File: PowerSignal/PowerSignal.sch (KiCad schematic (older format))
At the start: 12 parts, among them K1 POWER, P1 DIN_4_SHIELD, P2 BNC, U1 BUF634

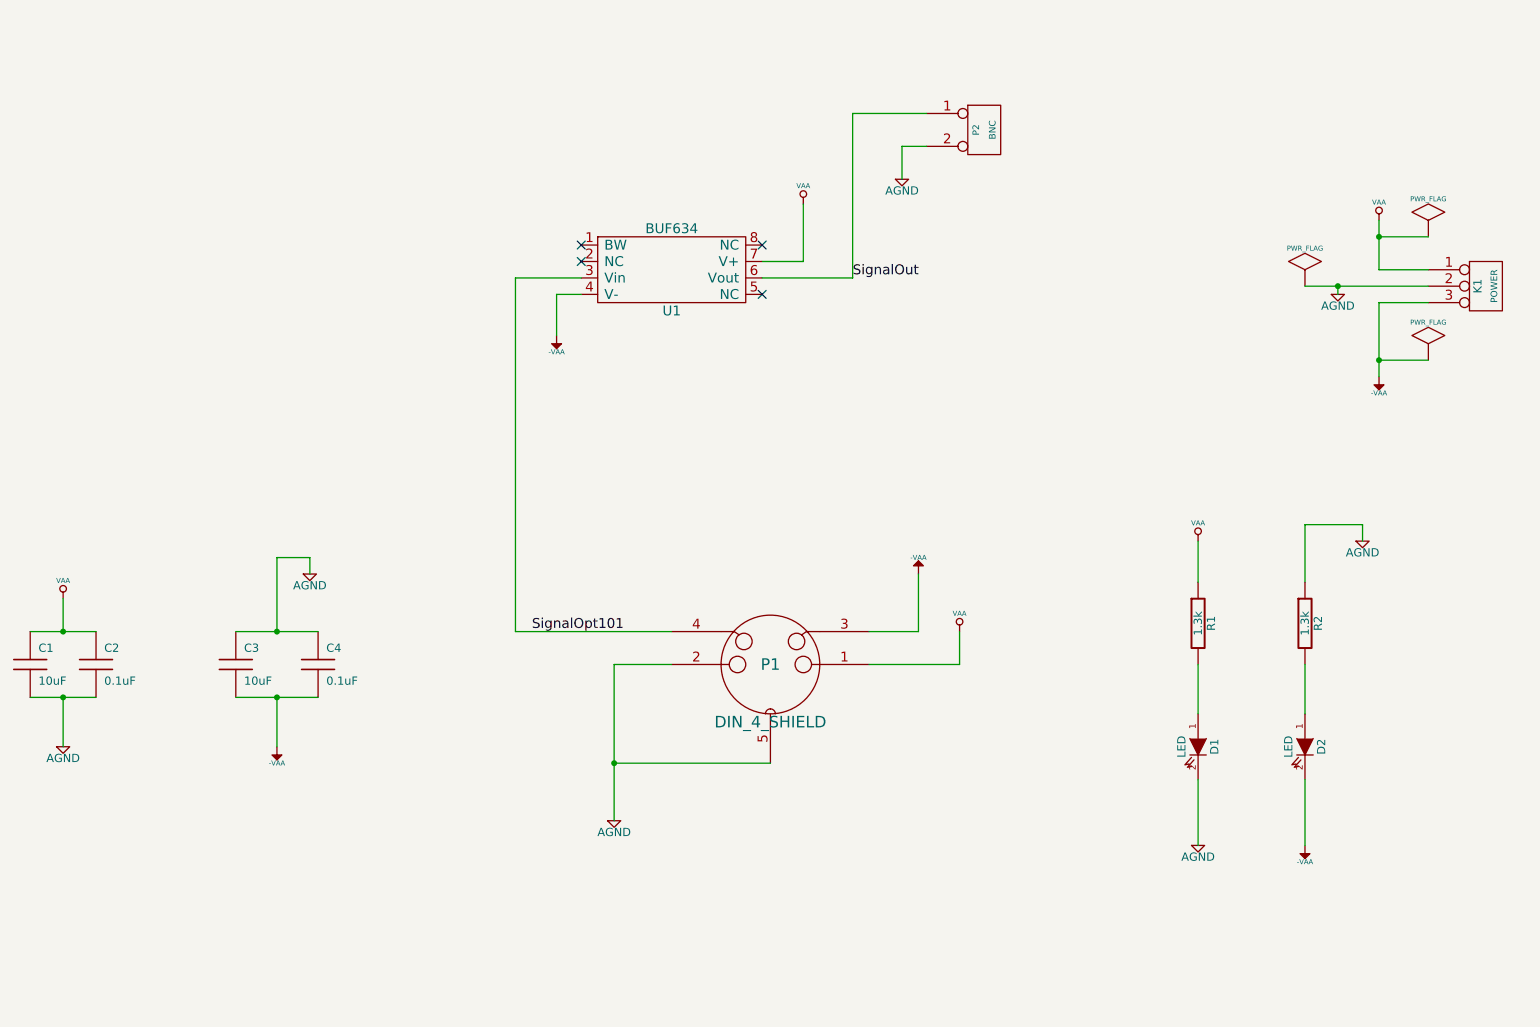
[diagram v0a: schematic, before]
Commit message: Designed PowerSupply board version 2
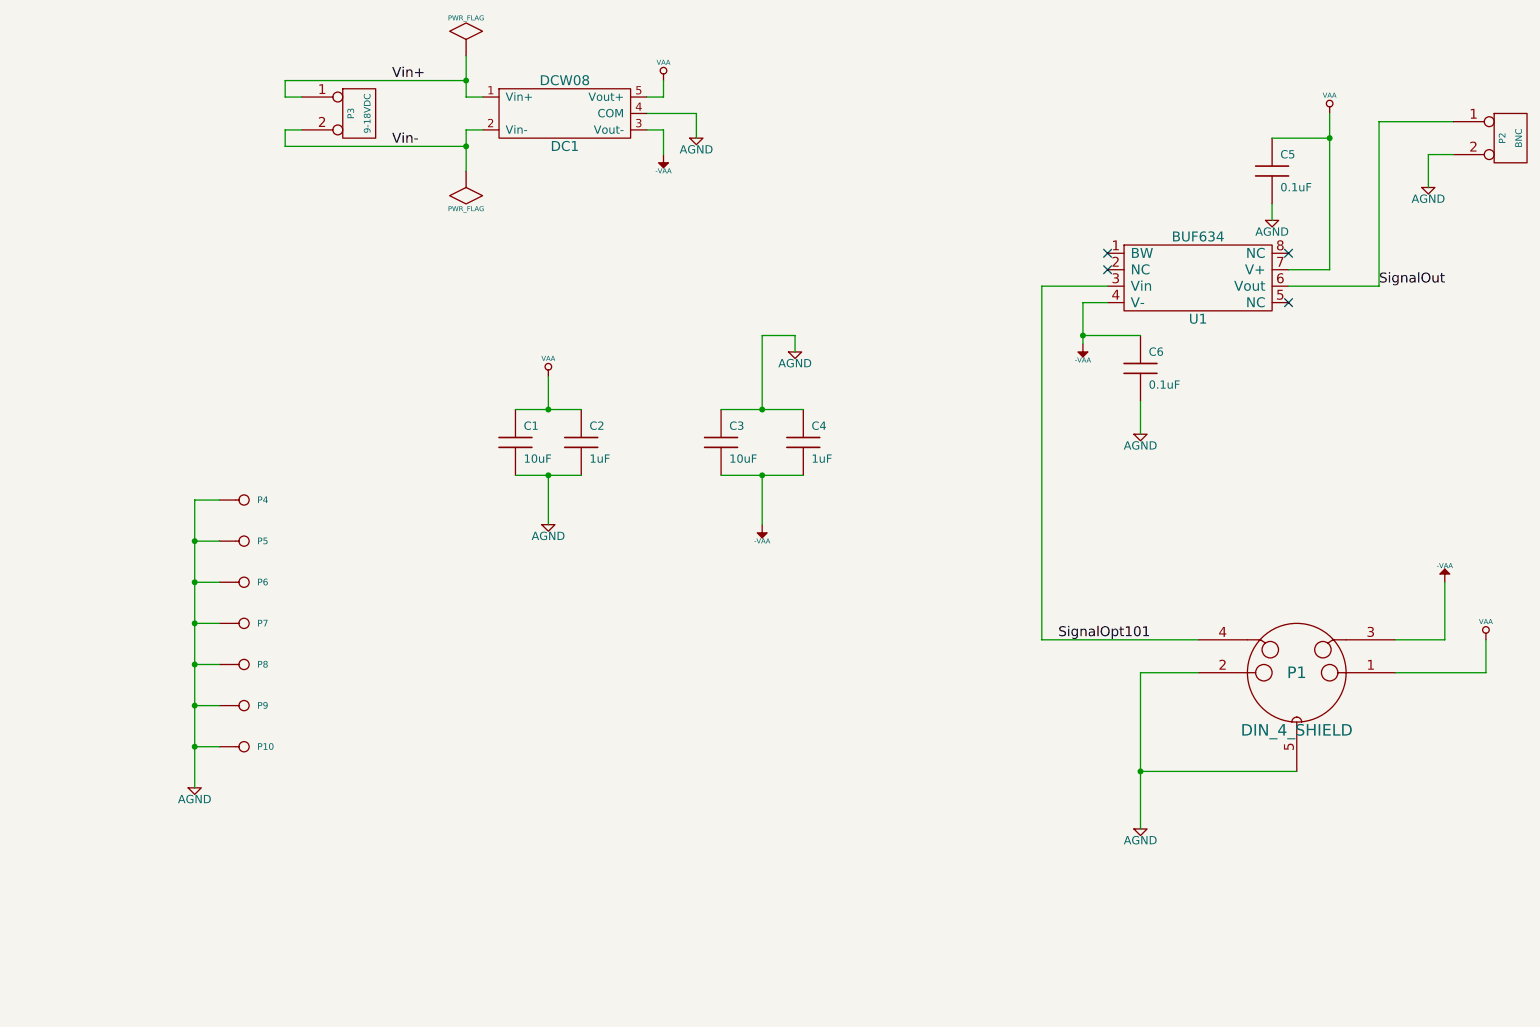
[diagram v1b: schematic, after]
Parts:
- removed D1, D2: LED, symbol LED
- removed K1: POWER, symbol CONN_3
- removed R1, R2: 1.3k, symbol R
- added C5, C6: 0.1uF, symbol C
- added DC1: DCW08, symbol DCW08
- added P10, P4, P5, P6, P7, P8, P9: CONN_1, symbol CONN_1
- added P3: 9-18VDC, symbol CONN_2
- C2, C4: value 0.1uF -> 1uF
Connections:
- net -VAA: now also C6.1, DC1.3 (Vout-)
- net AGND: now also C5.2, C6.2, DC1.4 (COM), P10.1, P4.1, P5.1, P6.1, P7.1, P8.1, P9.1
- net VAA: now also C5.1, DC1.5 (Vout+)
- new net Vin+: DC1.1 (Vin+), P3.1 (P1)
- new net Vin-: DC1.2 (Vin-), P3.2 (PM)
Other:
- moved on the sheet: C1, C2, C3, C4, P1, P2, U1

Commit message: Designed PowerSignal board version 2.1.  Now includes simple low-pass filter.
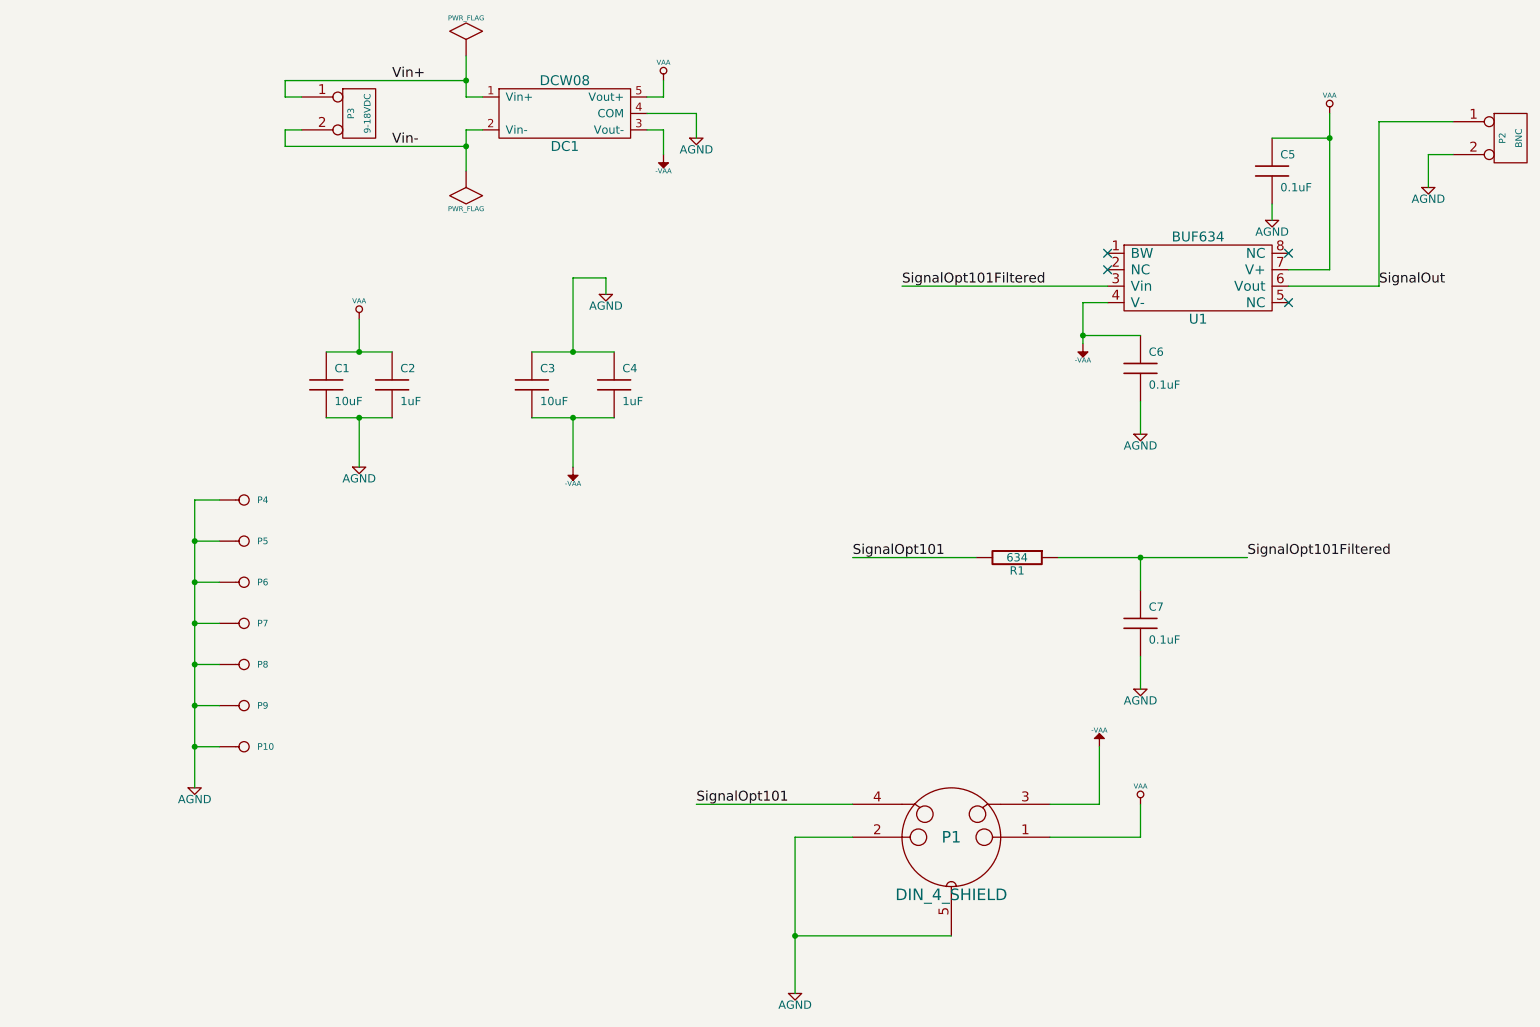
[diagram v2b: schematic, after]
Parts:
- added C7: 0.1uF, symbol C
- added R1: 634, symbol R
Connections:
- net AGND: now also C7.2
- net SignalOpt101: now also R1.2; no longer U1.3 (Vin)
- new net SignalOpt101Filtered: C7.1, R1.1, U1.3 (Vin)
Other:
- moved on the sheet: C1, C2, C3, C4, P1
